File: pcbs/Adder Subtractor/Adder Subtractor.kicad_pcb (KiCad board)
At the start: 2 copper layers, 50.8 x 71.1 mm, 5 parts, among them U1 74HC86, U2 74HC86, U3 74HC283, U4 74HC283

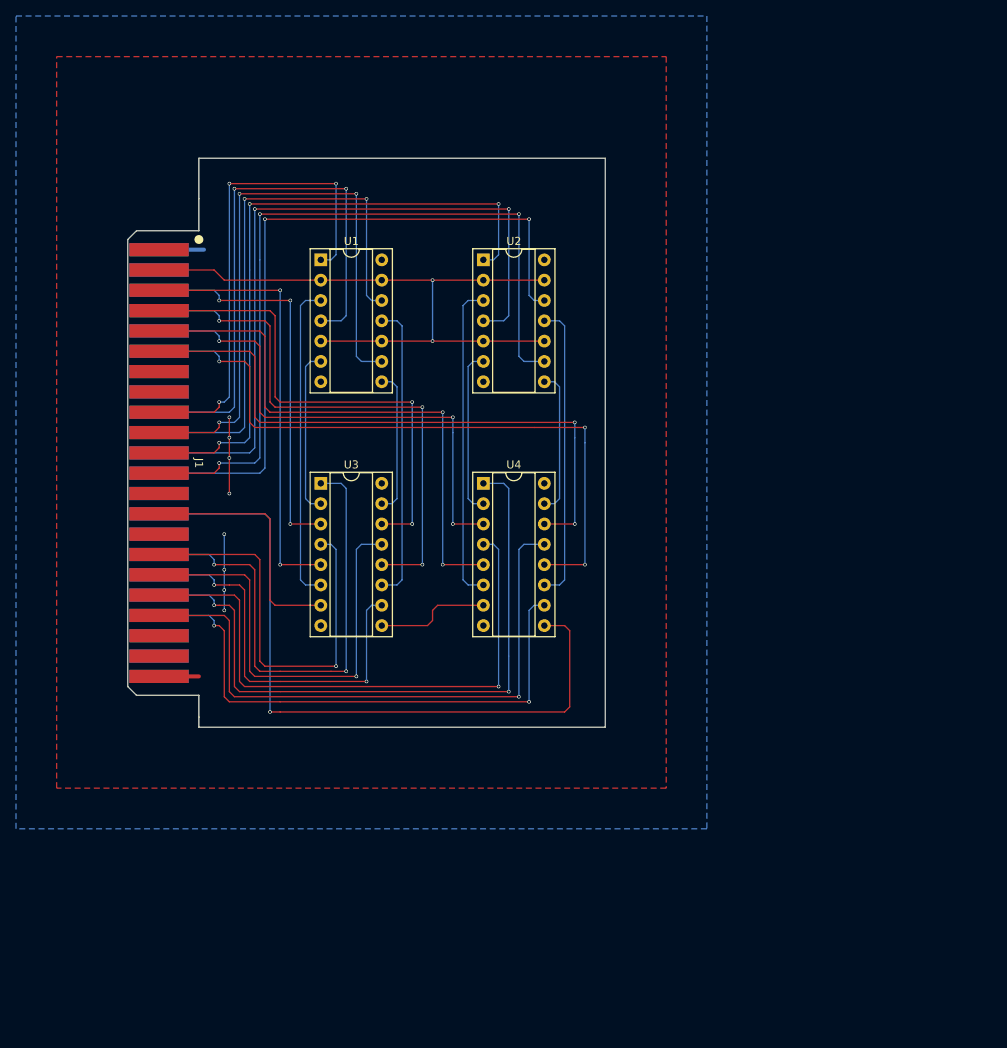
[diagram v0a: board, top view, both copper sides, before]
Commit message: Add output buffer
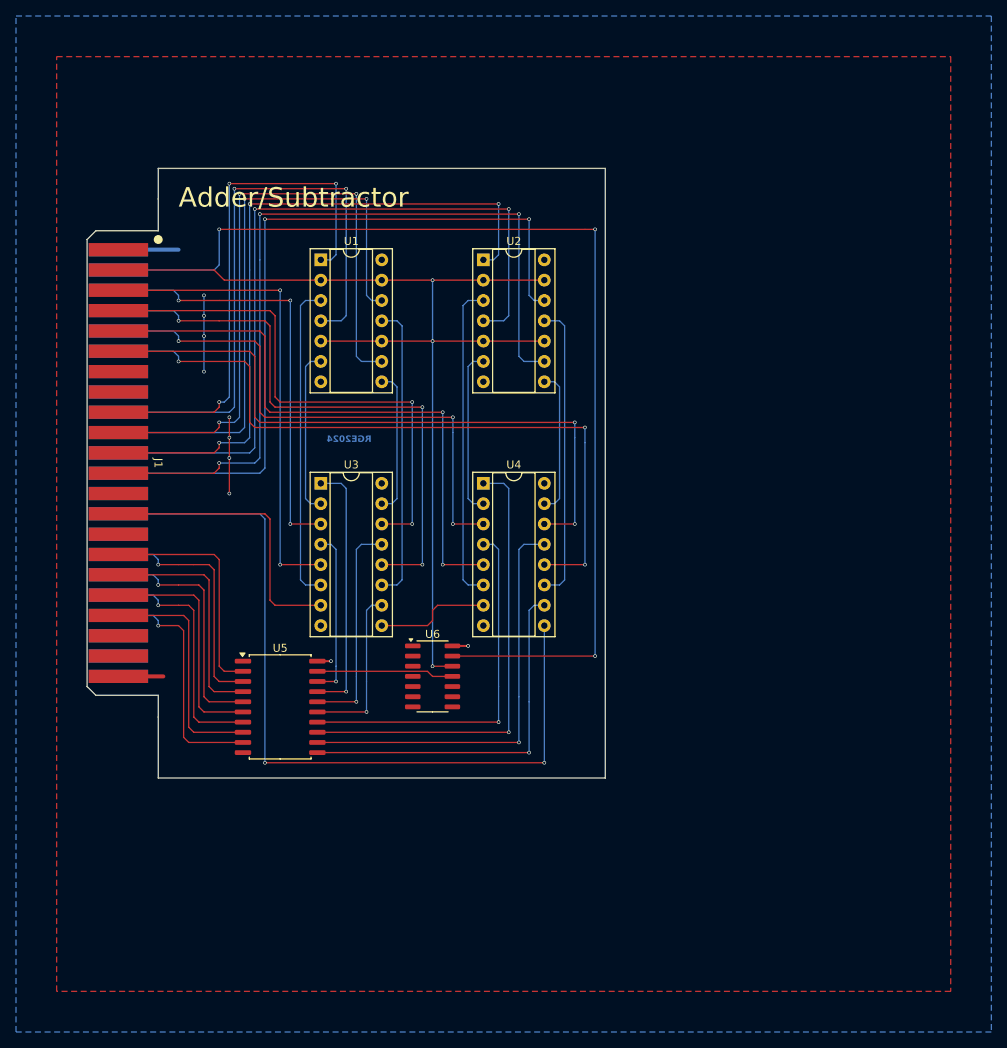
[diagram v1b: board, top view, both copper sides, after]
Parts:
- added U5: 74HC245, Package_SO:SOIC-20W_7.5x12.8mm_P1.27mm, F.Cu at (114.3, 111.8)
- added U6: 74HC08, Package_SO:SOIC-14_3.9x8.7mm_P1.27mm, F.Cu at (133.3, 108.0)
- moved J1 5.08 mm to (94.0, 81.3)
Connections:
- net /~{Add}/Sub renamed /~{Add}
- J1 pad A16: /Out0 -> /C0
- J1 pad A17: /Out2 -> /C2
- J1 pad A18: /Out4 -> /C4
- J1 pad A19: /Out6 -> /C6
- J1 pad B16: /Out1 -> /C1
- J1 pad B17: /Out3 -> /C3
- J1 pad B18: /Out5 -> /C5
- J1 pad B19: /Out7 -> /C7
- J1 pad B2: unconnected-(J1-PadB2) -> /~{Sub}
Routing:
- net /~{Sub}: track 0.00 -> 135.5 mm, vias 0 -> 3
- net /~{Add}: track 84.2 -> 132.4 mm, vias 2 -> 3
- net /Out0: track 52.1 -> 21.0 mm
- net /Out1: track 63.2 -> 32.4 mm, vias 2 -> 1
- net /C5: track 0.00 -> 30.3 mm, vias 0 -> 1
- net /C1: track 0.00 -> 30.3 mm, vias 0 -> 1
- net /C7: track 0.00 -> 30.3 mm, vias 0 -> 1
- net /C3: track 0.00 -> 30.3 mm, vias 0 -> 1
- net /C0: track 0.00 -> 29.4 mm
- net /C6: track 0.00 -> 29.4 mm
- net /C2: track 0.00 -> 29.4 mm
- net /C4: track 0.00 -> 29.4 mm
- net /Out2: track 55.9 -> 27.4 mm
- net /Out3: track 49.2 -> 21.0 mm, vias 2 -> 1
- net /Out4: track 72.4 -> 46.4 mm
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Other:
- board size 50.8 x 71.1 mm -> 55.9 x 76.2 mm
- board text added: "Adder/Subtractor"
- board text added: "JLCJLCJLCJLC"
- board text added: "RGE2024"

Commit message: Indicator LEDs
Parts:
- added D1: Blue, LED_SMD:LED_0603_1608Metric, F.Cu at (151.1, 58.4)
- added D2: Blue, LED_SMD:LED_0603_1608Metric, F.Cu at (151.1, 60.3)
- added R1: 4k7, Resistor_SMD:R_0603_1608Metric, F.Cu at (151.1, 56.5)
- added R2: 4k7, Resistor_SMD:R_0603_1608Metric, F.Cu at (151.1, 62.2)
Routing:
- net +5V: track 20.7 -> 25.0 mm, vias 6 -> 7
- net Net-(D2-A): track 0.00 -> 3.36 mm
- net Net-(D1-A): track 0.00 -> 3.36 mm
- net /~{Add}: track 132.4 -> 135.5 mm
- net /~{Sub}: track 135.5 -> 137.2 mm, vias 3 -> 4
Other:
- board size 55.9 x 76.2 mm -> 57.2 x 76.2 mm
- board text added: "Add"
- board text added: "Sub"

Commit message: Capacitors for Adder/Subtractor
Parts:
- added C1: C, Capacitor_SMD:C_0603_1608Metric, F.Cu at (127.0, 80.0)
- added C2: C, Capacitor_SMD:C_0603_1608Metric, F.Cu at (147.3, 80.0)
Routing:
- net +5V: track 25.0 -> 31.1 mm
